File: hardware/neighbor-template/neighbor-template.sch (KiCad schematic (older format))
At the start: 7 parts, among them J1 NEIGHBOR1, J2 NEIGHBOR2, J7 BONUS_ROW

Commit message: neighbors: pin header part selection
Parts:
- J1, J2: Description (none) -> CONN RCPT .100\" 40POS DUAL-ROW STACKING GOLD; Manufacturer (none) -> Samtec; Part Number (none) -> SSQ-120-23-G-D
- J7: Description (none) -> CONN RCPT .100\" 20POS SINGLE-ROW STACKING GOLD; Manufacturer (none) -> Samtec; Part Number (none) -> SSQ-120-23-G-S
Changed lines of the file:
@@
 F 2 "gsg-modules:HEADER-2x20" H 15750 1700 60  0001 C CNN
 F 3 "" H 15750 1700 60  0000 C CNN
+F 4 "Samtec" H 15750 2650 60  0001 C CNN "Manufacturer"
+F 5 "SSQ-120-23-G-D" H 15750 2650 60  0001 C CNN "Part Number"
+F 6 "CONN RCPT .100\" 40POS DUAL-ROW STACKING GOLD" H 15750 2650 60  0001 C CNN "Description"
 	1    15750 2650
 	1    0    0    -1
@@
 F 2 "gsg-modules:HEADER-2x20" H 15750 4300 60  0001 C CNN
 F 3 "" H 15750 4300 60  0000 C CNN
+F 4 "Samtec" H 15750 5250 60  0001 C CNN "Manufacturer"
+F 5 "SSQ-120-23-G-D" H 15750 5250 60  0001 C CNN "Part Number"
+F 6 "CONN RCPT .100\" 40POS DUAL-ROW STACKING GOLD" H 15750 5250 60  0001 C CNN "Description"
 	1    15750 5250
 	1    0    0    -1
@@
 F 2 "gsg-modules:HEADER-1x20" H 15200 7000 60  0001 C CNN
 F 3 "" H 15200 7000 60  0000 C CNN
+F 4 "Samtec" H 15200 7000 60  0001 C CNN "Manufacturer"
+F 5 "SSQ-120-23-G-S" H 15200 7000 60  0001 C CNN "Part Number"
+F 6 "CONN RCPT .100\" 20POS SINGLE-ROW STACKING GOLD" H 15200 7000 60  0001 C CNN "Description"
 	1    15200 7000
 	0    -1   -1   0

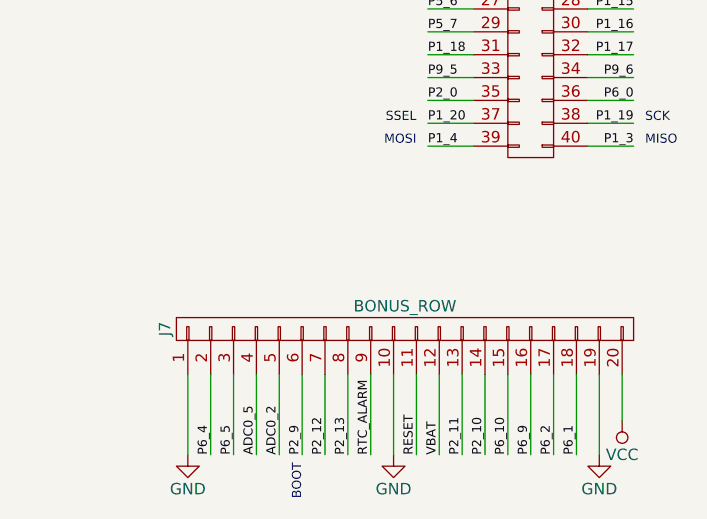
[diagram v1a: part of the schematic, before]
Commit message: neighbors: alternate header selection
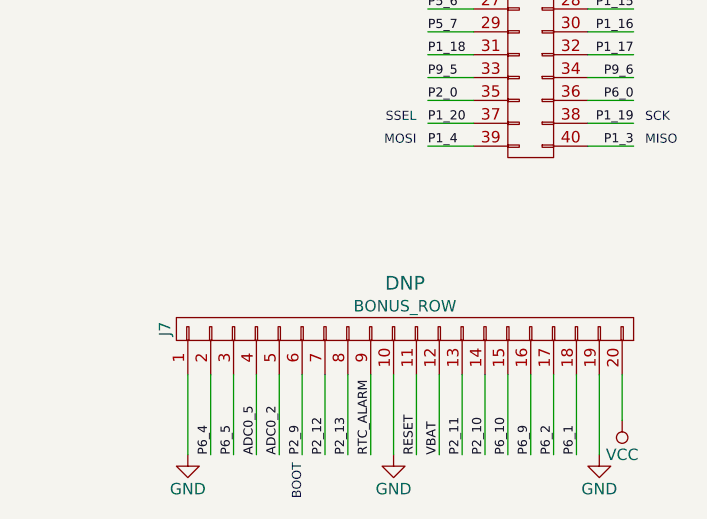
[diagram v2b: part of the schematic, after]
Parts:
- J1, J2: Note (none) -> Alternate: https://www.adafruit.com/products/2223
- J7: Note (none) -> DNP
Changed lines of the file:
@@
 F 5 "SSQ-120-23-G-D" H 15750 2650 60  0001 C CNN "Part Number"
 F 6 "CONN RCPT .100\" 40POS DUAL-ROW STACKING GOLD" H 15750 2650 60  0001 C CNN "Description"
+F 7 "Alternate: https://www.adafruit.com/products/2223" H 15750 2650 60  0001 C CNN "Note"
 	1    15750 2650
 	1    0    0    -1
@@
 F 5 "SSQ-120-23-G-D" H 15750 5250 60  0001 C CNN "Part Number"
 F 6 "CONN RCPT .100\" 40POS DUAL-ROW STACKING GOLD" H 15750 5250 60  0001 C CNN "Description"
+F 7 "Alternate: https://www.adafruit.com/products/2223" H 15750 5250 60  0001 C CNN "Note"
 	1    15750 5250
 	1    0    0    -1
@@
 F 5 "SSQ-120-23-G-S" H 15200 7000 60  0001 C CNN "Part Number"
 F 6 "CONN RCPT .100\" 20POS SINGLE-ROW STACKING GOLD" H 15200 7000 60  0001 C CNN "Description"
+F 7 "DNP" V 15400 7000 60  0000 C CNN "Note"
 	1    15200 7000
 	0    -1   -1   0

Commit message: Added jasmine neighbor
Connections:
- net VBUS: no longer J2.2 (P2)
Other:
- moved on the sheet: J2
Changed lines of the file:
@@
 Comment4 ""
 $EndDescr
-Text Label 15300 2300 0    40   ~ 0
+Text Label 15300 2550 0    40   ~ 0
 P2_8
 $Comp
 L CONN_02X20 J2
 U 1 1 55EAB4B7
-P 15750 2650
-F 0 "J2" H 15750 3700 50  0000 C CNN
-F 1 "NEIGHBOR2" V 15750 2650 50  0000 C CNN
-F 2 "gsg-modules:HEADER-2x20" H 15750 1700 60  0001 C CNN
-F 3 "" H 15750 1700 60  0000 C CNN
-F 4 "Samtec" H 15750 2650 60  0001 C CNN "Manufacturer"
-F 5 "SSQ-120-23-G-D" H 15750 2650 60  0001 C CNN "Part Number"
-F 6 "CONN RCPT .100\" 40POS DUAL-ROW STACKING GOLD" H 15750 2650 60  0001 C CNN "Description"
-F 7 "Alternate: https://www.adafruit.com/products/2223" H 15750 2650 60  0001 C CNN "Note"
-	1    15750 2650
+P 15750 2900
+F 0 "J2" H 15750 3950 50  0000 C CNN
+F 1 "NEIGHBOR2" V 15750 2900 50  0000 C CNN
+F 2 "gsg-modules:HEADER-2x20" H 15750 1950 60  0001 C CNN
+F 3 "" H 15750 1950 60  0000 C CNN
+F 4 "Samtec" H 15750 2900 60  0001 C CNN "Manufacturer"
+F 5 "SSQ-120-23-G-D" H 15750 2900 60  0001 C CNN "Part Number"
+F 6 "CONN RCPT .100\" 40POS DUAL-ROW STACKING GOLD" H 15750 2900 60  0001 C CNN "Description"
+F 7 "Alternate: https://www.adafruit.com/products/2223" H 15750 2900 60  0001 C CNN "Note"
+	1    15750 2900
 	1    0    0    -1
 $EndComp
@@
 L GND #PWR059
 U 1 1 55EACE84
-P 15300 1700
-F 0 "#PWR059" H 15300 1450 50  0001 C CNN
-F 1 "GND" H 15300 1550 50  0000 C CNN
-F 2 "" H 15300 1700 60  0000 C CNN
-F 3 "" H 15300 1700 60  0000 C CNN
-	1    15300 1700
+P 15300 1950
+F 0 "#PWR059" H 15300 1700 50  0001 C CNN
+F 1 "GND" H 15300 1800 50  0000 C CNN
+F 2 "" H 15300 1950 60  0000 C CNN
+F 3 "" H 15300 1950 60  0000 C CNN
+	1    15300 1950
 	0    1    1    0
 $EndComp
@@
 	0    1    1    0
 $EndComp
-Text Label 16200 1700 2    40   ~ 0
+Text Label 16200 1950 2    40   ~ 0
 VBUS
 $Comp
@@
 Text Notes 15250 6100 2    40   ~ 0
 SSEL
-Text Label 16300 3600 2    40   ~ 0
+Text Label 16300 3850 2    40   ~ 0
 I2C0_SCL
-Text Label 15200 3600 0    40   ~ 0
+Text Label 15200 3850 0    40   ~ 0
 I2C0_SDA
-Text Label 16200 3400 2    40   ~ 0
+Text Label 16200 3650 2    40   ~ 0
 P6_3
-Text Label 15300 3400 0    40   ~ 0
+Text Label 15300 3650 0    40   ~ 0
 P2_1
-Text Label 16200 3300 2    40   ~ 0
+Text Label 16200 3550 2    40   ~ 0
 P6_6
-Text Label 15300 3300 0    40   ~ 0
+Text Label 15300 3550 0    40   ~ 0
 P2_2
-Text Label 15300 3200 0    40   ~ 0
+Text Label 15300 3450 0    40   ~ 0
 P6_7
-Text Label 15300 3100 0    40   ~ 0
+Text Label 15300 3350 0    40   ~ 0
 P6_8
-Text Label 16200 2600 2    40   ~ 0
+Text Label 16200 2850 2    40   ~ 0
 P2_3
-Text Label 15300 2600 0    40   ~ 0
+Text Label 15300 2850 0    40   ~ 0
 P2_4
-Text Label 16200 2500 2    40   ~ 0
+Text Label 16200 2750 2    40   ~ 0
 P2_5
-Text Label 15300 2400 0    40   ~ 0
+Text Label 15300 2650 0    40   ~ 0
 P2_6
-Text Label 16200 2200 2    40   ~ 0
+Text Label 16200 2450 2    40   ~ 0
 CLK2
-Text Label 15300 3000 0    40   ~ 0
+Text Label 15300 3250 0    40   ~ 0
 P7_0
-Text Label 16200 2900 2    40   ~ 0
+Text Label 16200 3150 2    40   ~ 0
 P3_0
-Text Label 15300 2900 0    40   ~ 0
+Text Label 15300 3150 0    40   ~ 0
 P7_1
-Text Label 16200 2800 2    40   ~ 0
+Text Label 16200 3050 2    40   ~ 0
 P3_1
-Text Label 15300 2800 0    40   ~ 0
+Text Label 15300 3050 0    40   ~ 0
 P7_2
-Text Label 16200 2700 2    40   ~ 0
+Text Label 16200 2950 2    40   ~ 0
 P3_2
-Text Label 16200 3200 2    40   ~ 0
+Text Label 16200 3450 2    40   ~ 0
 P3_3
-Text Label 16200 3000 2    40   ~ 0
+Text Label 16200 3250 2    40   ~ 0
 P3_4
-Text Label 15300 2700 0    40   ~ 0
+Text Label 15300 2950 0    40   ~ 0
 PF_4
-Text Label 15300 3500 0    40   ~ 0
+Text Label 15300 3750 0    40   ~ 0
 P3_5
-Text Label 16200 3500 2    40   ~ 0
+Text Label 16200 3750 2    40   ~ 0
 P3_6
-Text Label 16200 3100 2    40   ~ 0
+Text Label 16200 3350 2    40   ~ 0
 P3_7
-Text Label 16200 2400 2    40   ~ 0
+Text Label 16200 2650 2    40   ~ 0
 P7_7
-Text Label 16200 1800 2    40   ~ 0
+Text Label 16200 2050 2    40   ~ 0
 P4_0
-Text Label 15250 1900 0    40   ~ 0
+Text Label 15250 2150 0    40   ~ 0
 ADC0_0
-Text Label 15300 2100 0    40   ~ 0
+Text Label 15300 2350 0    40   ~ 0
 P4_3
-Text Label 16200 2000 2    40   ~ 0
+Text Label 16200 2250 2    40   ~ 0
 P4_2
-Text Label 15300 2000 0    40   ~ 0
+Text Label 15300 2250 0    40   ~ 0
 P4_4
-Text Label 16200 1900 2    40   ~ 0
+Text Label 16200 2150 2    40   ~ 0
 P4_5
-Text Label 16200 2100 2    40   ~ 0
+Text Label 16200 2350 2    40   ~ 0
 P4_6
-Text Label 15300 2200 0    40   ~ 0
+Text Label 15300 2450 0    40   ~ 0
 P4_7
-Text Label 15300 1800 0    40   ~ 0
+Text Label 15300 2050 0    40   ~ 0
 P4_8
-Text Label 15200 2500 0    40   ~ 0
+Text Label 15200 2750 0    40   ~ 0
 WAKEUP0
-Text Label 16200 2300 2    40   ~ 0
+Text Label 16200 2550 2    40   ~ 0
 P2_7
-Text Notes 16350 2300 2    40   ~ 0
+Text Notes 16350 2550 2    40   ~ 0
 ISP
-Text Notes 15150 2300 0    40   ~ 0
+Text Notes 15150 2550 0    40   ~ 0
 DFU
 Text Notes 16250 4700 0    40   ~ 0
@@
 	15300 4400 15500 4400
 Wire Wire Line
-	16200 1700 16000 1700
-Wire Wire Line
-	15300 1700 15500 1700
+	15300 1950 15500 1950
 Wire Wire Line
 	15300 4500 15500 4500
@@
 	16200 6100 16000 6100
 Wire Wire Line
-	15300 3500 15500 3500
-Wire Wire Line
-	16000 3500 16200 3500
-Wire Wire Line
-	16200 3400 16000 3400
-Wire Wire Line
-	15500 3400 15300 3400
-Wire Wire Line
-	15300 3300 15500 3300
-Wire Wire Line
-	16200 3300 16000 3300
-Wire Wire Line
-	16200 3200 16000 3200
-Wire Wire Line
-	16200 3100 16000 3100
-Wire Wire Line
-	15500 3200 15300 3200
-Wire Wire Line
-	15300 3100 15500 3100
-Wire Wire Line
-	15500 3000 15300 3000
-Wire Wire Line
-	16200 2900 16000 2900
-Wire Wire Line
-	16300 3600 16000 3600
-Wire Wire Line
-	15500 3600 15200 3600
-Wire Wire Line
-	16200 3000 16000 3000
-Wire Wire Line
-	15300 2900 15500 2900
-Wire Wire Line
-	15300 2800 15500 2800
-Wire Wire Line
-	16200 2800 16000 2800
-Wire Wire Line
-	16200 2700 16000 2700
-Wire Wire Line
-	15300 2700 15500 2700
-Wire Wire Line
-	16200 2600 16000 2600
-Wire Wire Line
-	15500 2600 15300 2600
-Wire Wire Line
-	16200 2500 16000 2500
-Wire Wire Line
-	15500 2500 15200 2500
-Wire Wire Line
-	15300 2400 15500 2400
-Wire Wire Line
-	16200 2400 16000 2400
-Wire Wire Line
-	16200 2300 16000 2300
-Wire Wire Line
-	15300 2300 15500 2300
-Wire Wire Line
-	16200 2200 16000 2200
-Wire Wire Line
-	15300 2200 15500 2200
-Wire Wire Line
-	16200 2100 16000 2100
-Wire Wire Line
-	15300 2100 15500 2100
-Wire Wire Line
-	16200 2000 16000 2000
-Wire Wire Line
-	15500 2000 15300 2000
-Wire Wire Line
-	15250 1900 15500 1900
-Wire Wire Line
-	16200 1900 16000 1900
-Wire Wire Line
-	15300 1800 15500 1800
-Wire Wire Line
-	16000 1800 16200 1800
+	15300 3750 15500 3750
+Wire Wire Line
+	16000 3750 16200 3750
+Wire Wire Line
+	16200 3650 16000 3650
+Wire Wire Line
+	15500 3650 15300 3650
+Wire Wire Line
+	15300 3550 15500 3550
+Wire Wire Line
+	16200 3550 16000 3550
+Wire Wire Line
+	16200 3450 16000 3450
+Wire Wire Line
+	16200 3350 16000 3350
+Wire Wire Line
+	15500 3450 15300 3450
+Wire Wire Line
+	15300 3350 15500 3350
+Wire Wire Line
+	15500 3250 15300 3250
+Wire Wire Line
+	16200 3150 16000 3150
+Wire Wire Line
+	16300 3850 16000 3850
+Wire Wire Line
+	15500 3850 15200 3850
+Wire Wire Line
+	16200 3250 16000 3250
+Wire Wire Line
+	15300 3150 15500 3150
+Wire Wire Line
+	15300 3050 15500 3050
+Wire Wire Line
+	16200 3050 16000 3050
+Wire Wire Line
+	16200 2950 16000 2950
+Wire Wire Line
+	15300 2950 15500 2950
+Wire Wire Line
+	16200 2850 16000 2850
+Wire Wire Line
+	15500 2850 15300 2850
+Wire Wire Line
+	16200 2750 16000 2750
+Wire Wire Line
+	15500 2750 15200 2750
+Wire Wire Line
+	15300 2650 15500 2650
+Wire Wire Line
+	16200 2650 16000 2650
+Wire Wire Line
+	16200 2550 16000 2550
+Wire Wire Line
+	15300 2550 15500 2550
+Wire Wire Line
+	16200 2450 16000 2450
+Wire Wire Line
+	15300 2450 15500 2450
+Wire Wire Line
+	16200 2350 16000 2350
+Wire Wire Line
+	15300 2350 15500 2350
+Wire Wire Line
+	16200 2250 16000 2250
+Wire Wire Line
+	15500 2250 15300 2250
+Wire Wire Line
+	15250 2150 15500 2150
+Wire Wire Line
+	16200 2150 16000 2150
+Wire Wire Line
+	15300 2050 15500 2050
+Wire Wire Line
+	16000 2050 16200 2050
 Wire Wire Line
 	15950 7550 15950 7200
